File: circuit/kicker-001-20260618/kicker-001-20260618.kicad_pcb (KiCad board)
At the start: 2 copper layers, 71.4 x 59.3 mm, 60 parts, among them J1 Solenoid_{Stroke}, J2 Solenoid_{Chip}, J3 Drribler_{Front}, J4 Conn_Relay, J6 Voltmeter, Q1 BSS138, Q2 TJ15S06M3L, Q3 Q_Photo_CE, Q4 MTB010N06RJ3, Q5 MTB010N06RJ3, U1 NOT, U10 TLP2361, U11 AND, U12 AND, U2 TLP2361, U3 XL6009E1, U4 NOT, U5 NOT, U6 DRV8874, U7 NOT, U8 NOT, U9 TLP2361

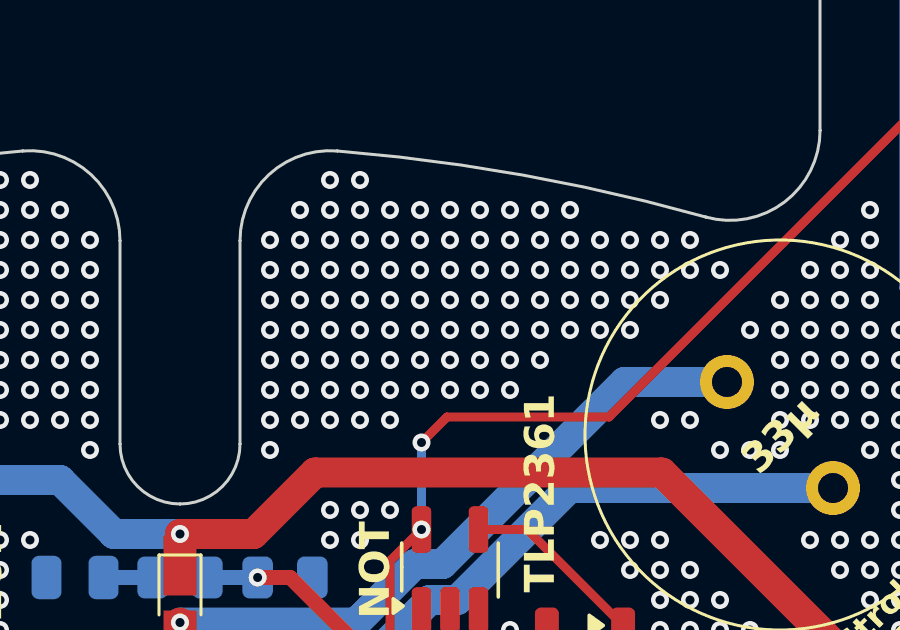
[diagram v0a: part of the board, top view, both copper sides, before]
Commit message: Update キッカー基板のQRコード上にあったビアを最低限にして可読性を高めた
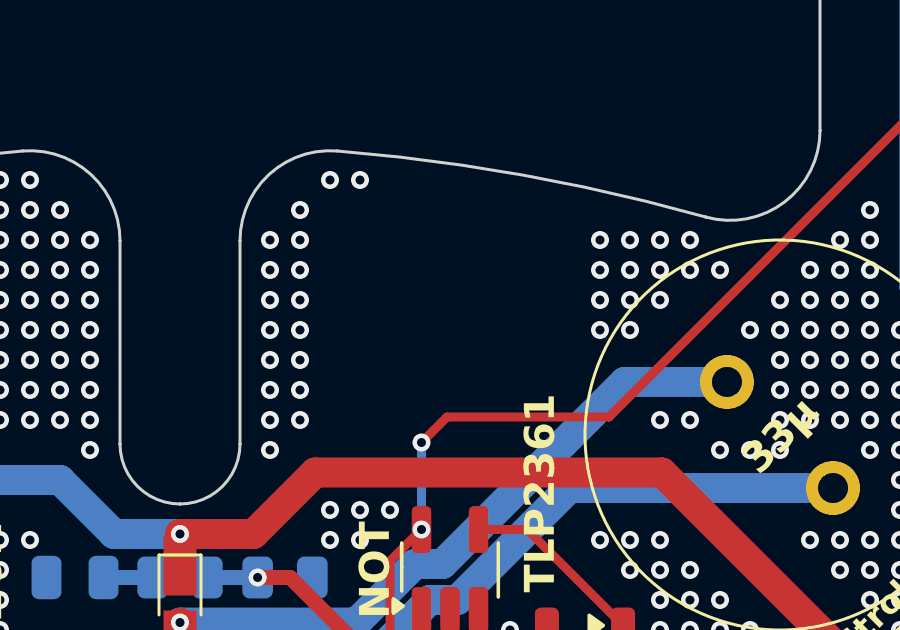
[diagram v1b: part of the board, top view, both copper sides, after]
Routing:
- net GND: vias 497 -> 434
